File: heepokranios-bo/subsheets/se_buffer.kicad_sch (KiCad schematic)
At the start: 16 parts, among them IC13 ADA4945-1ACPZ-R7, J14 Conn_01x03

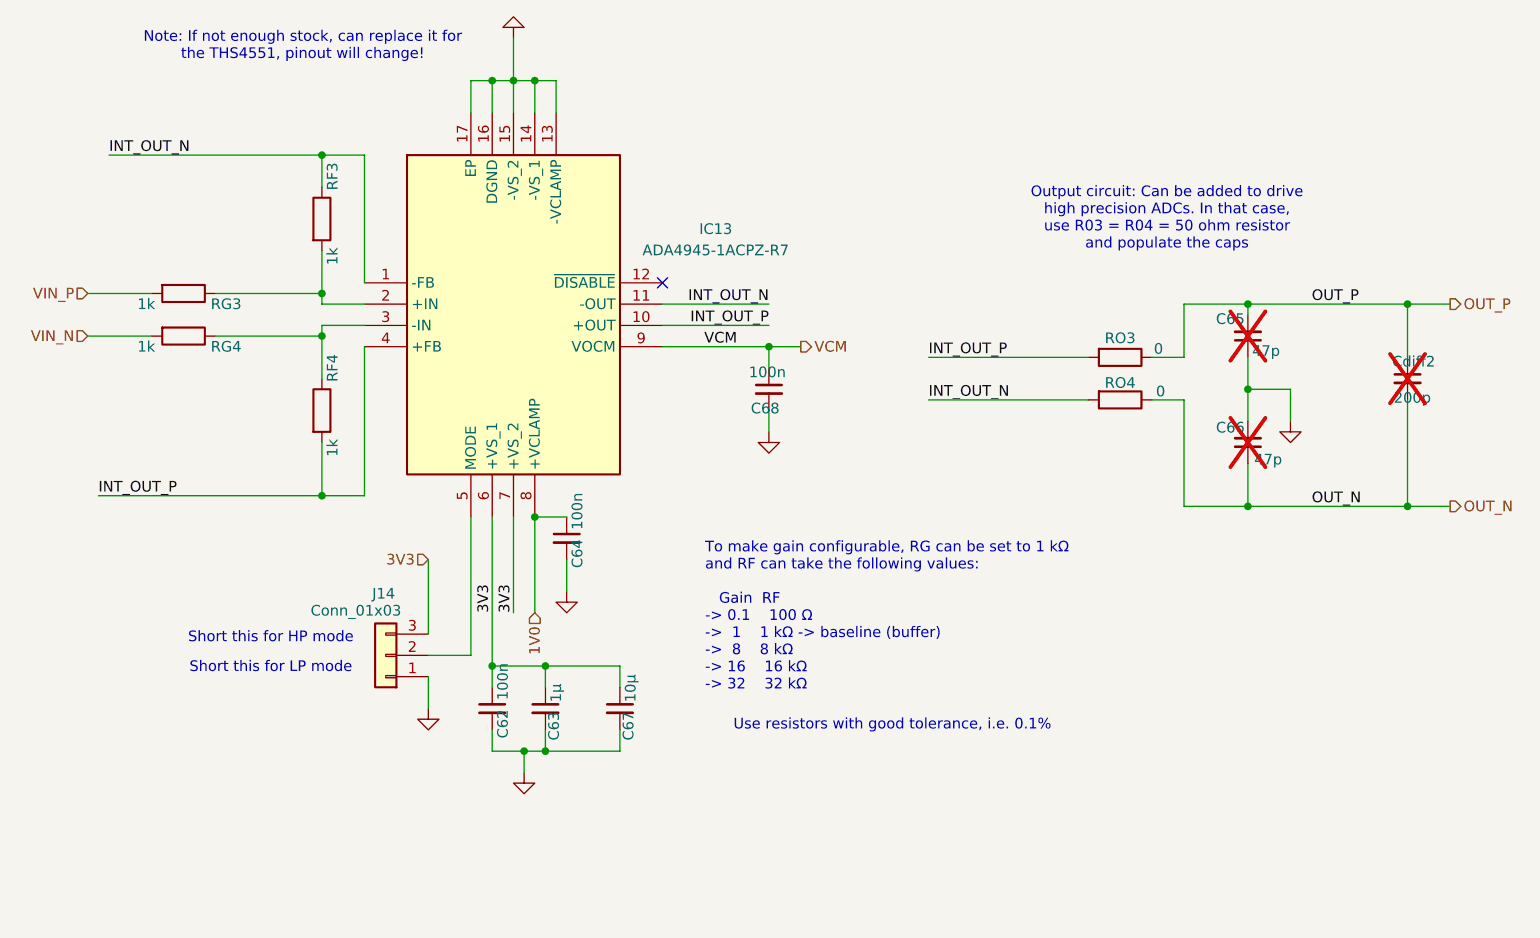
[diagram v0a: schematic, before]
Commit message: Added floorplan and outline of breakout board
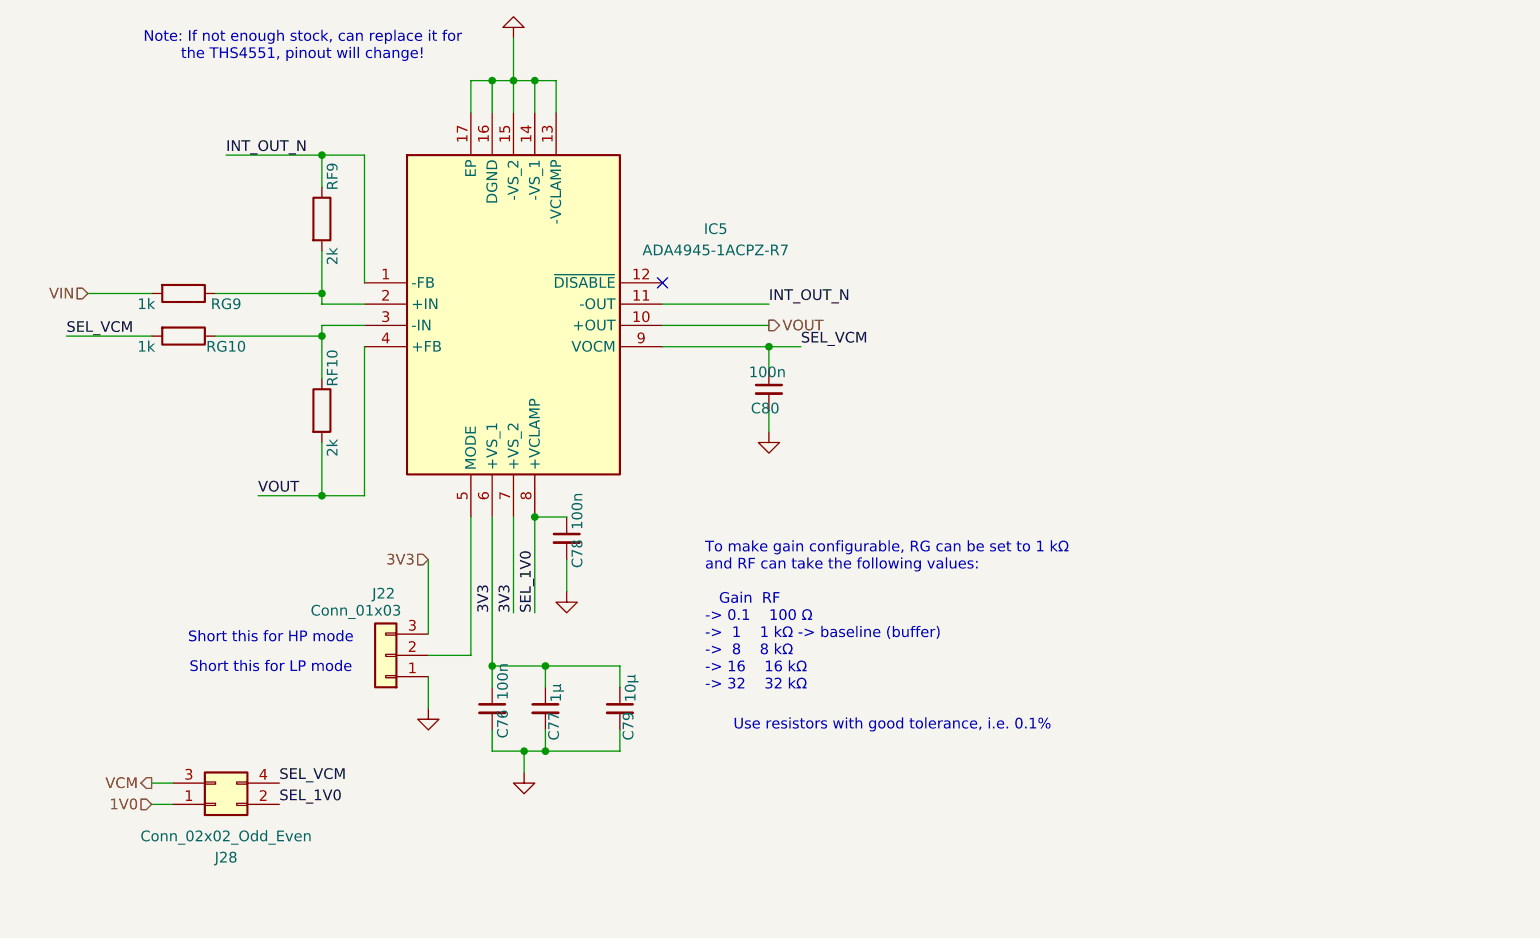
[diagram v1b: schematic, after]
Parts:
- removed C62, C64, C68: 100n, Capacitor_SMD:C_0603_1608Metric, symbol Device:C_Small
- removed C63: 1μ, Capacitor_SMD:C_0603_1608Metric, symbol Device:C_Small
- removed C65, C66: 47p, Capacitor_SMD:C_0603_1608Metric, symbol Device:C_Small
- removed C67: 10μ, Capacitor_SMD:C_0603_1608Metric, symbol Device:C_Small
- removed Cdiff2: 200p, Capacitor_SMD:C_0603_1608Metric, symbol Device:C_Small
- removed IC13: ADA4945-1ACPZ-R7, KiCad:QFN50P300X300X80-17N-D, symbol ADA4945-1ACPZ-R7:ADA4945-1ACPZ-R7
- removed J14: Conn_01x03, Connector_PinHeader_2.54mm:PinHeader_1x03_P2.54mm_Vertical, symbol Connector_Generic:Conn_01x03
- removed RF3, RF4, RG3, RG4: 1k, Resistor_SMD:R_0603_1608Metric, symbol Device:R
- removed RO3, RO4: 0, Resistor_SMD:R_0603_1608Metric, symbol Device:R
- added C76, C78, C80: 100n, Capacitor_SMD:C_0603_1608Metric, symbol Device:C_Small
- added C77: 1μ, Capacitor_SMD:C_0603_1608Metric, symbol Device:C_Small
- added C79: 10μ, Capacitor_SMD:C_0603_1608Metric, symbol Device:C_Small
- added IC5: ADA4945-1ACPZ-R7, heepokranios-bo-library:QFN50P300X300X80-17N-D, symbol ADA4945-1ACPZ-R7:ADA4945-1ACPZ-R7
- added J22: Conn_01x03, Connector_PinHeader_2.54mm:PinHeader_1x03_P2.54mm_Vertical, symbol Connector_Generic:Conn_01x03
- added J28: Conn_02x02_Odd_Even, Connector_PinHeader_2.54mm:PinHeader_2x02_P2.54mm_Vertical, symbol Connector_Generic:Conn_02x02_Odd_Even
- added RF10, RF9: 2k, Resistor_SMD:R_0603_1608Metric, symbol Device:R
- added RG10, RG9: 1k, Resistor_SMD:R_0603_1608Metric, symbol Device:R
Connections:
- net 1V0: now also J28.1 (Pin_1)
- net 3V3: now also C76.1, C77.1, C79.1, IC5.6 (+VS_1), IC5.7 (+VS_2), J22.3 (Pin_3)
- net GND: now also C76.2, C77.2, C78.2, C79.2, C80.2, IC5.13 (-VCLAMP), IC5.14 (-VS_1), IC5.15 (-VS_2), IC5.16 (DGND), IC5.17 (EP), J22.1 (Pin_1)
- net INT_OUT_N: now also IC5.1 (-FB), IC5.11 (-OUT), RF9.1
- net VCM: now also J28.3 (Pin_3)
- new net: IC5.2 (+IN), RF9.2, RG9.1
- new net: IC5.3 (-IN), RF10.1, RG10.1
- new net: IC5.5 (MODE), J22.2 (Pin_2)
- new net SEL_1V0: C78.1, IC5.8 (+VCLAMP), J28.2 (Pin_2)
- new net SEL_VCM: C80.1, IC5.9 (VOCM), J28.4 (Pin_4), RG10.2
- new net VIN: RG9.2
- new net VOUT: IC5.10 (+OUT), IC5.4 (+FB), RF10.2
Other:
- note removed: "Output circuit: Can be added to drive high precision ADCs. In that case, use R03 = R04 = 50 ohm resistor and populate the caps"

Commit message: Changed in sch and board the fully diff amplifiers within the buffers to the THS4551IRGTR as there was no more stock of the one from Analog Devices
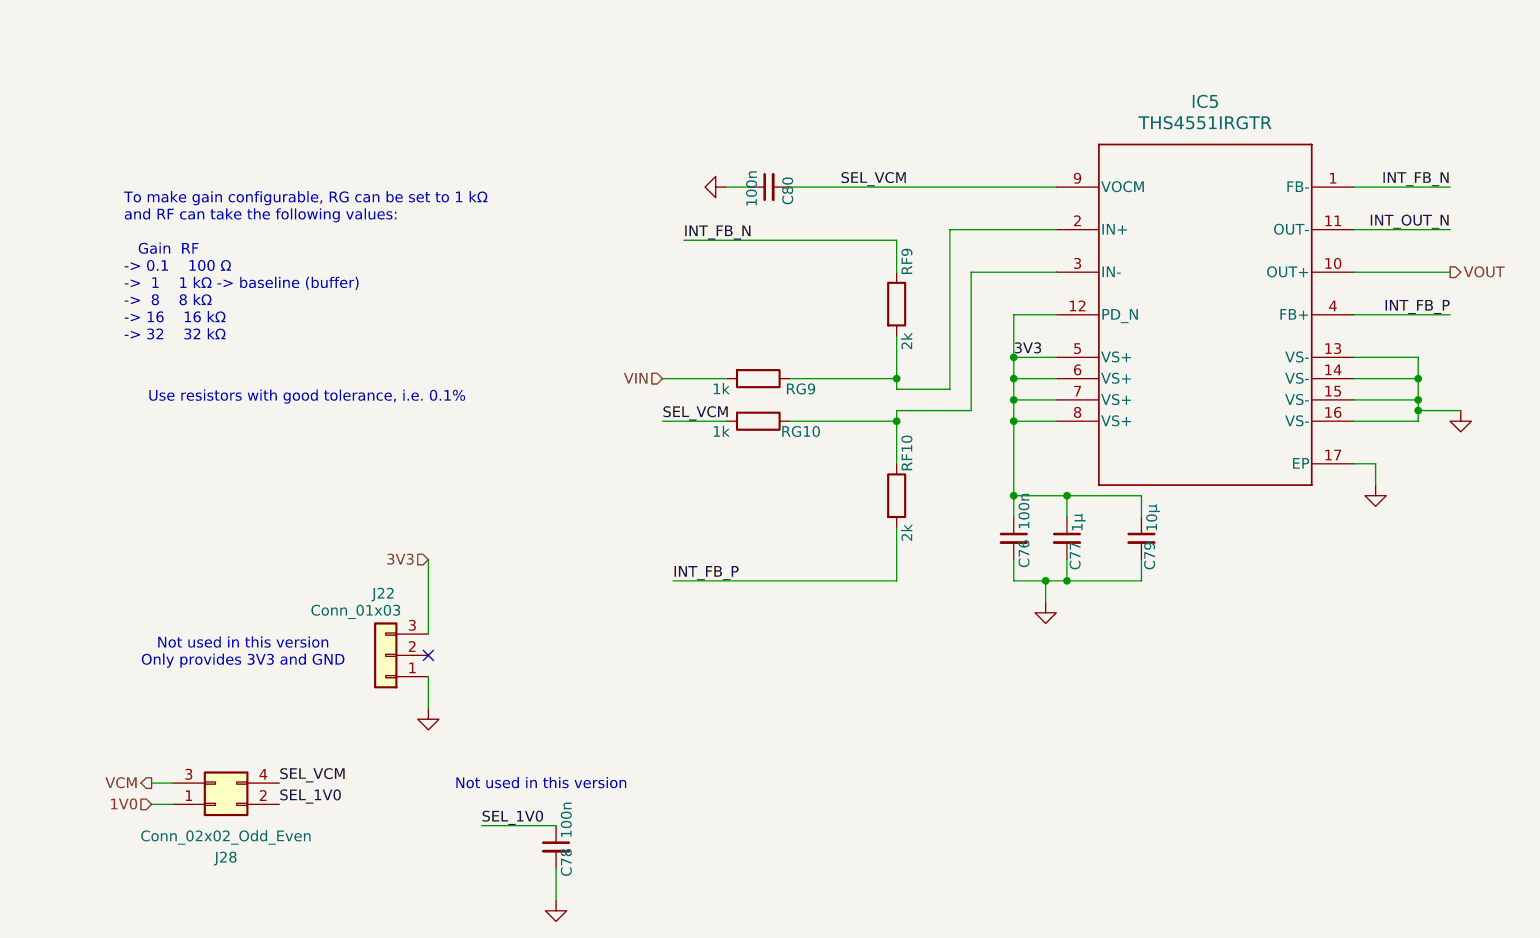
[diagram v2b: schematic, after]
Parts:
- removed IC5: ADA4945-1ACPZ-R7, heepokranios-bo-library:QFN50P300X300X80-17N-D, symbol ADA4945-1ACPZ-R7:ADA4945-1ACPZ-R7
- added IC5: THS4551IRGTR, RGT0016C, symbol heepokranios-bo-library:THS4551IRGTR
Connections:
- net 3V3: now also IC5.12 (PD_N), IC5.5 (VS+), IC5.6 (VS+), IC5.7 (VS+), IC5.8 (VS+)
- net GND: now also C80.1, IC5.13 (VS-), IC5.14 (VS-), IC5.15 (VS-), IC5.16 (VS-), IC5.17 (EP); no longer C80.2
- net INT_OUT_N: now also IC5.11 (OUT-); no longer RF9.1
- net SEL_VCM: now also C80.2, IC5.9 (VOCM); no longer C80.1
- net VOUT: now also IC5.10 (OUT+); no longer RF10.2
- net at RF9.2, RG9.1: now also IC5.2 (IN+)
- net at RF10.1, RG10.1: now also IC5.3 (IN-)
- new net INT_FB_N: IC5.1 (FB-), RF9.1
- new net INT_FB_P: IC5.4 (FB+), RF10.2
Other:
- note added: "Not used in this version"
- note added: "Not used in this version Only provides 3V3 and GND"
- note removed: "Note: If not enough stock, can replace it for the THS4551, pinout will change!"
- note removed: "Short this for HP mode"
- note removed: "Short this for LP mode"
- moved on the sheet: C76, C77, C78, C79, C80, RF10, RF9, RG10, RG9
